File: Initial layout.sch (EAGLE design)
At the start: 32 parts, among them U2 TPS54540DDARQ1

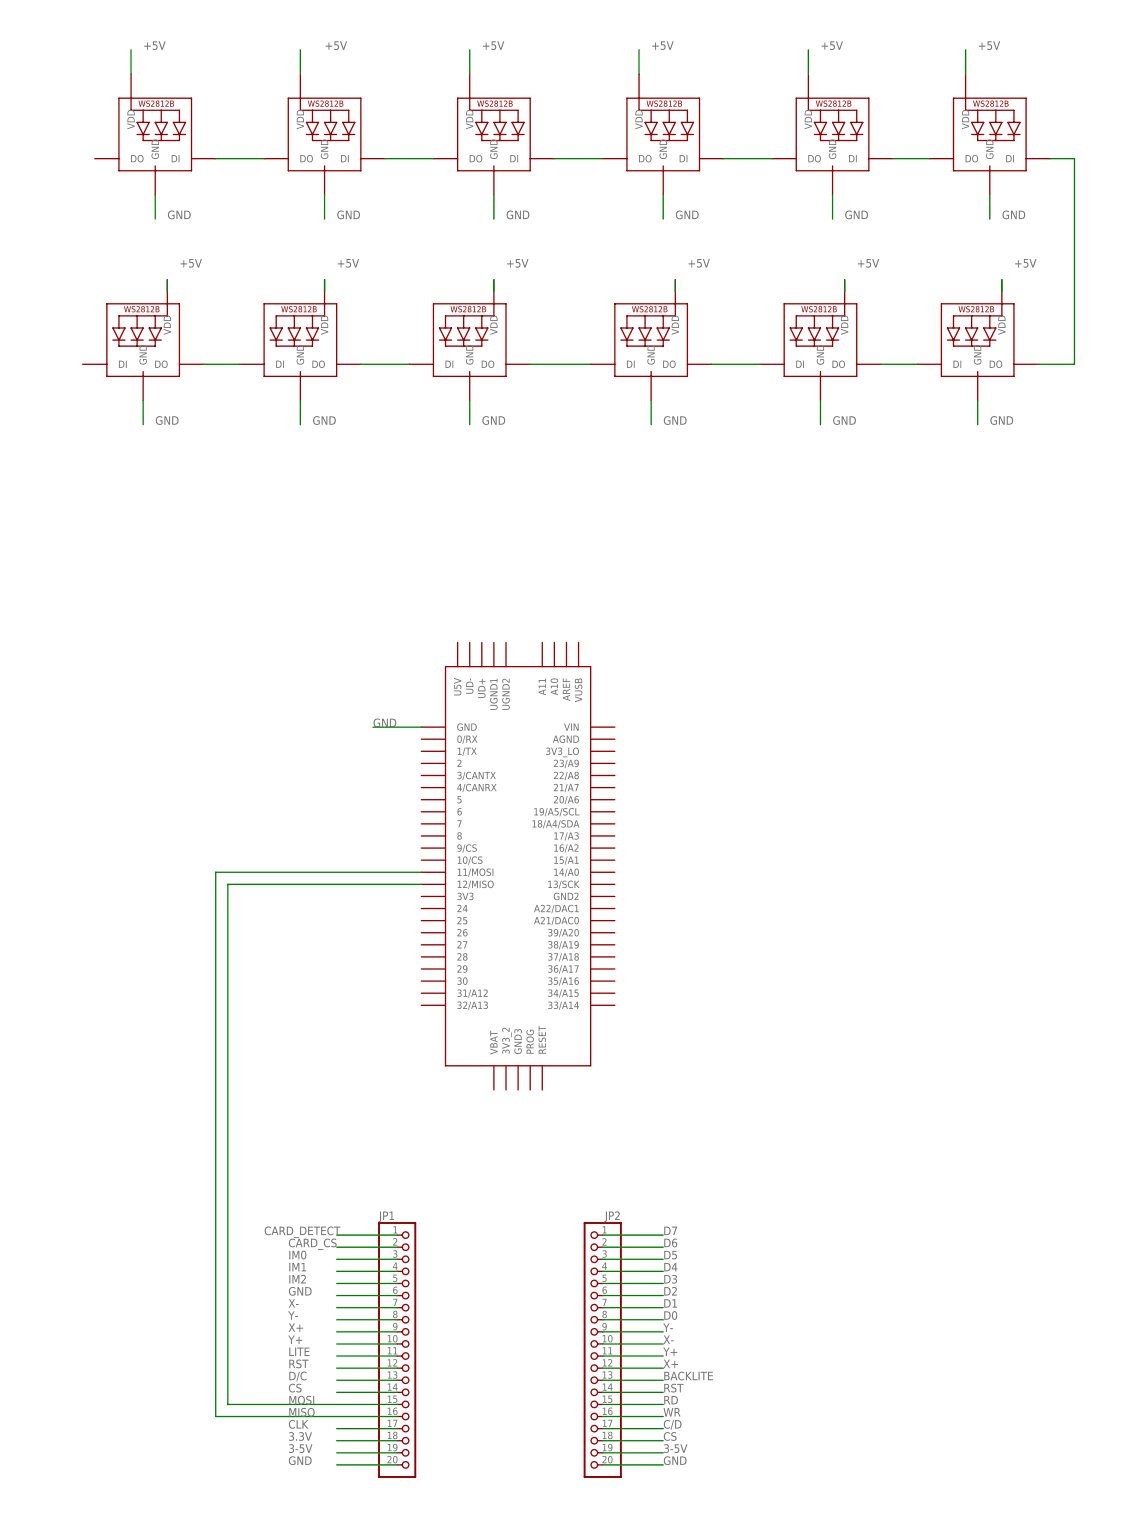
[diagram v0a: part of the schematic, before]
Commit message: Worked on schematic. Connected some wires
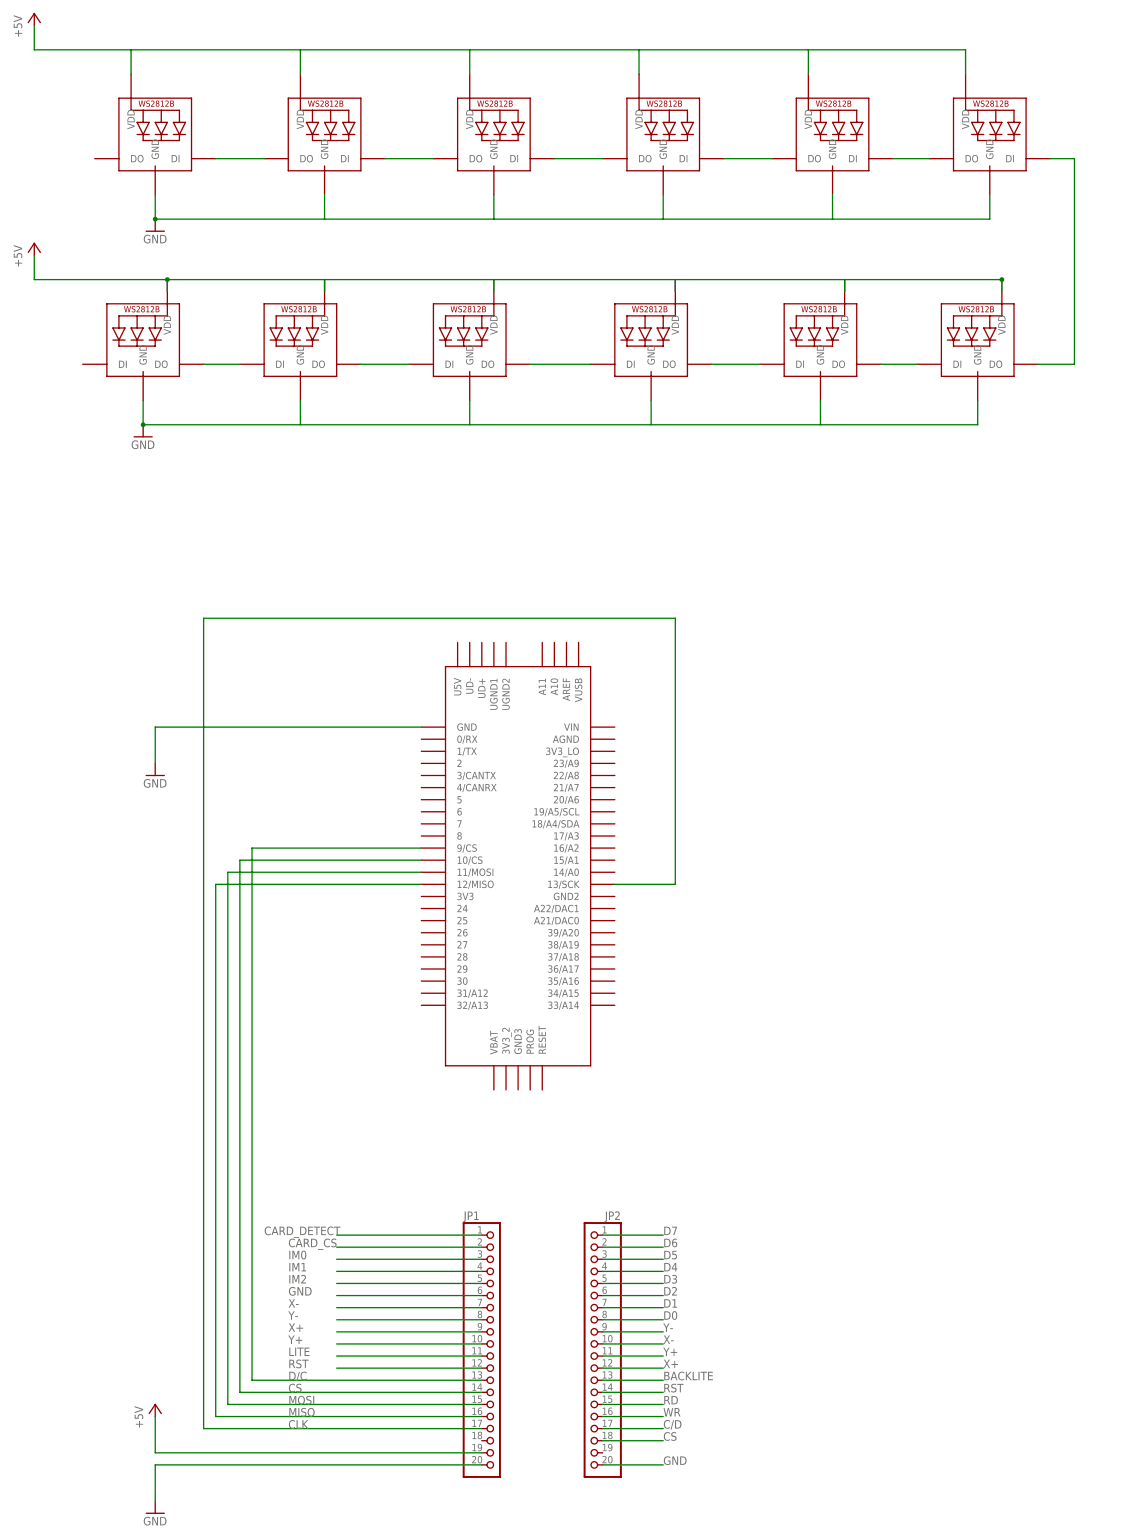
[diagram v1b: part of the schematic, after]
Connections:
- removed net 3-5V: JP1.19, JP2.19
- removed net 3.3V: JP1.18
- new net N$1: LED2.GND
- net +5V: now also JP1.19
- net CLK: now also U$2.13/SCK
- net CS: now also U$2.10/CS
- net D/C: now also U$2.9/CS
- net GND: no longer LED2.GND
- net MISO: now also U$2.12/MISO; no longer U$2.11/MOSI
- net MOSI: now also U$2.11/MOSI; no longer U$2.12/MISO
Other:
- moved on the sheet: JP1

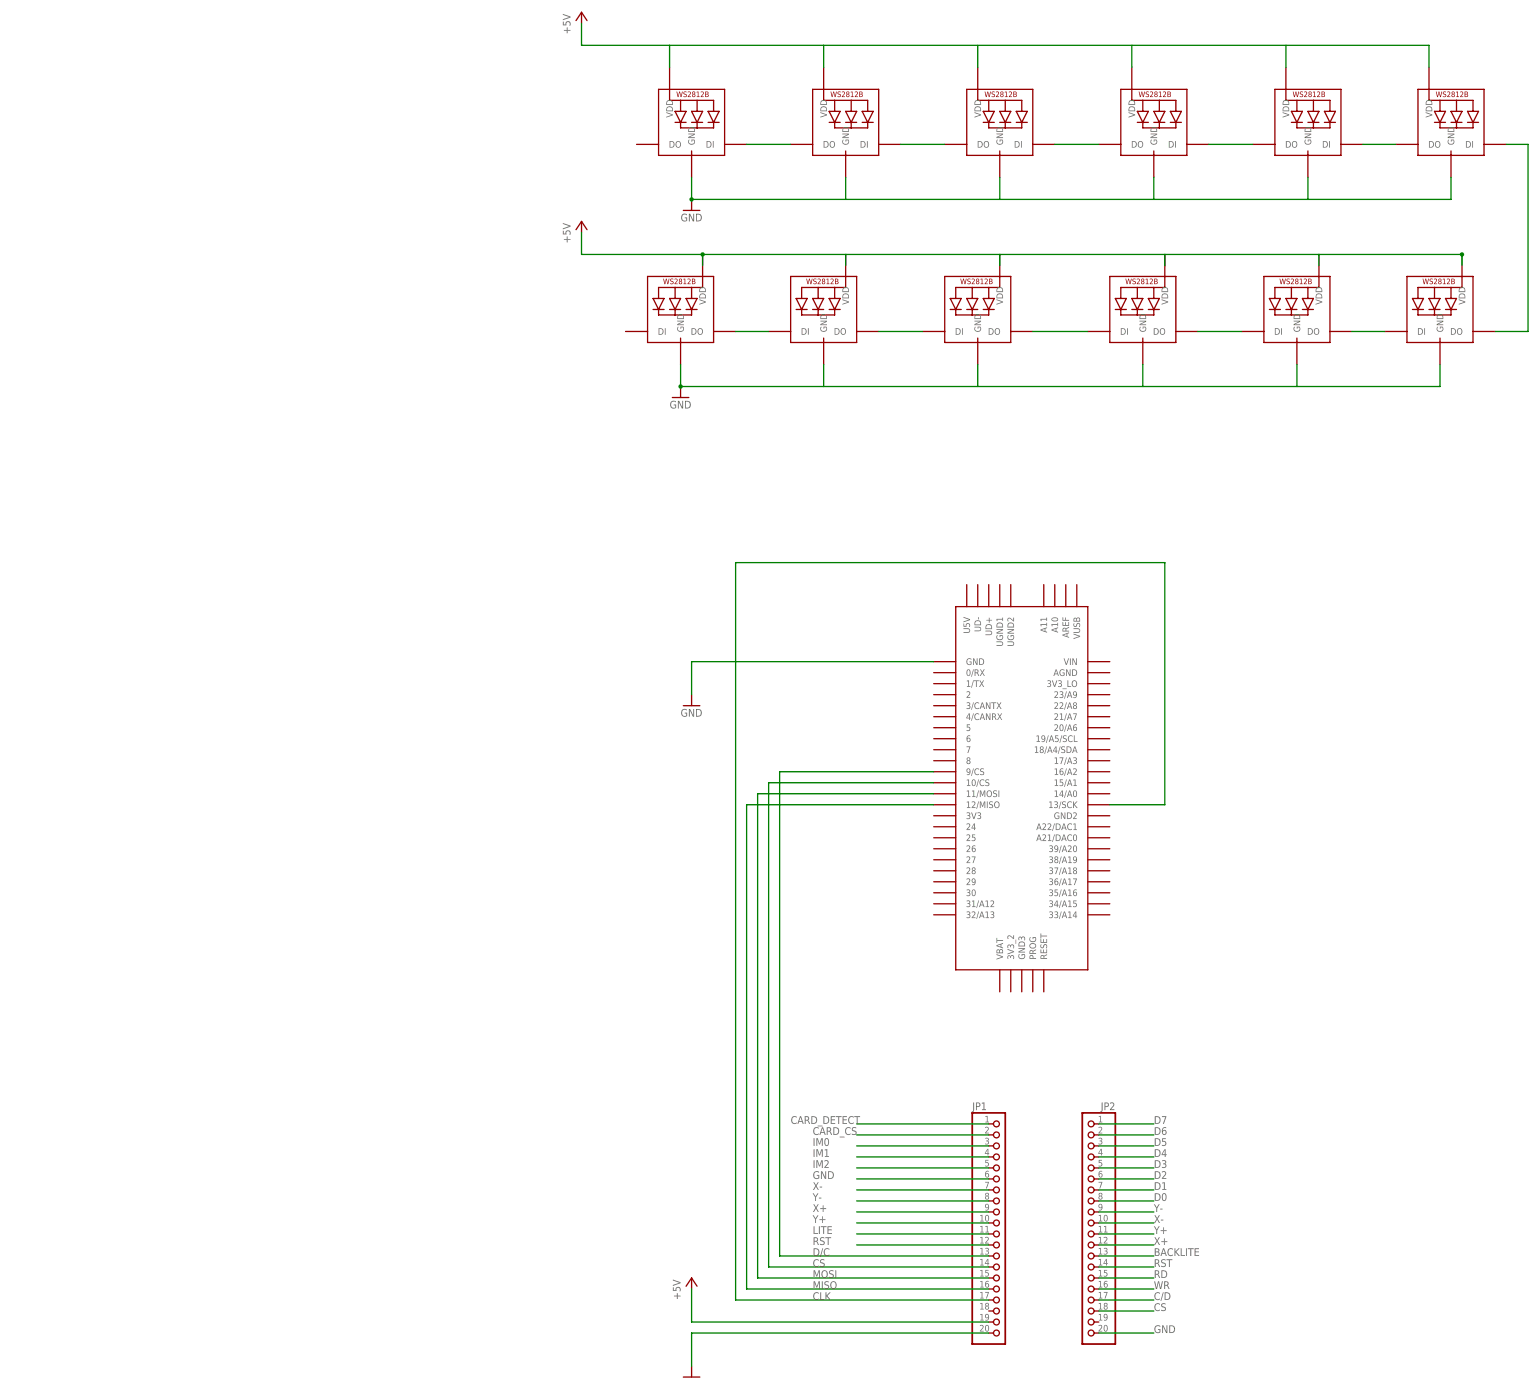
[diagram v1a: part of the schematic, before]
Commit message: Added some connectors.
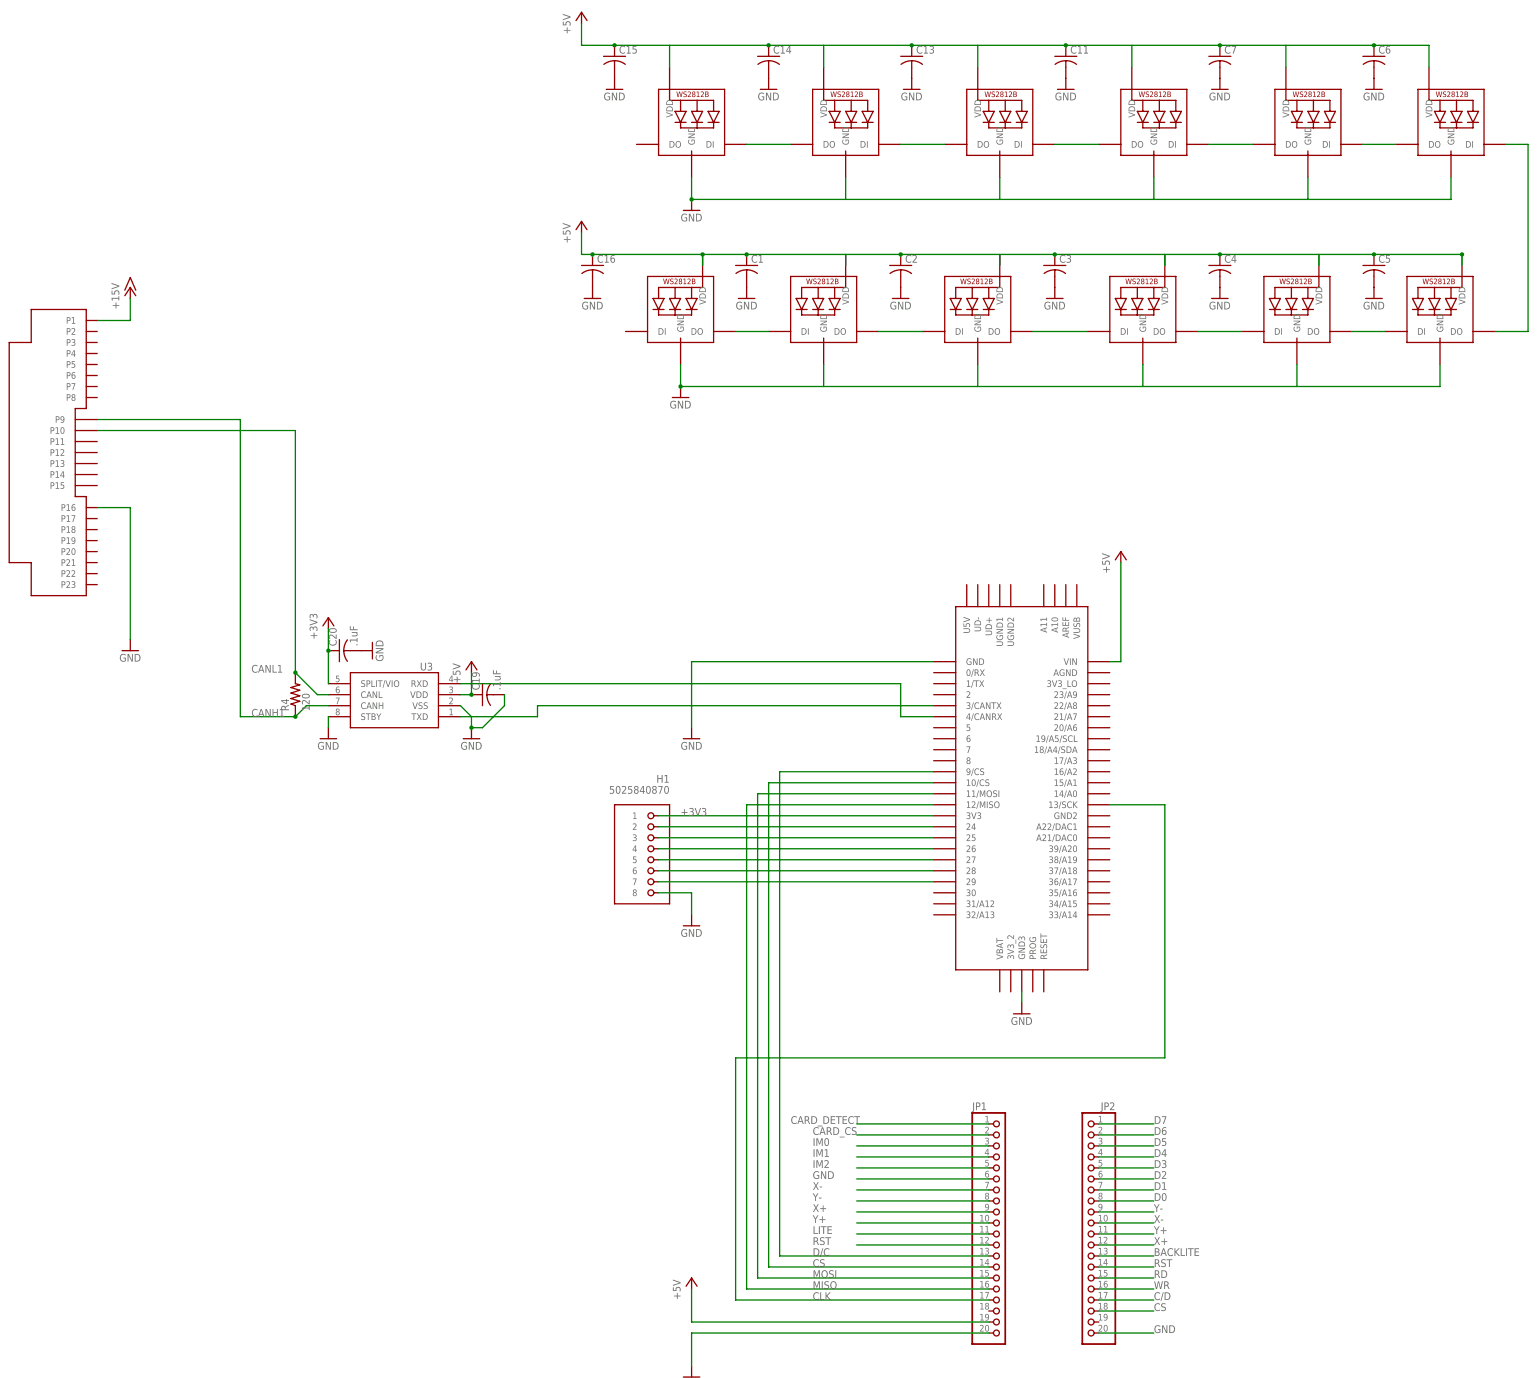
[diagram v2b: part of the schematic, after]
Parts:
- added C1, C11, C13, C14, C15, C16, C2, C3, C4, C5, C6, C7: (no value), rcl:C-USC0402
- added C19, C20: .1uF, rcl:C-USC0805
- added H1: 5025840870, FormE:MOLEX_CLICKMATE-8-VERTICAL
- added R4: 120, rcl:R-US_R0805
- added U$1: TE-776200-1, FormE:TE-776200-1
- added U3: (no value), FormE:MCP256X-SOIC
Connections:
- new net +3V3: C20.1, H1.1, U$2.3V3, U3.SPLIT/VIO
- new net CANH1: R4.1, U$1.P9, U3.CANH
- new net CANL1: R4.2, U$1.P10, U3.CANL
- new net N$11: H1.2, U$2.24
- new net N$13: H1.3, U$2.25
- new net N$15: H1.4, U$2.26
- new net N$17: H1.5, U$2.27
- new net N$18: H1.6, U$2.28
- new net N$19: H1.7, U$2.29
- new net N$25: U$2.4/CANRX, U3.RXD
- new net N$26: U$2.3/CANTX, U3.TXD
- net +15V: now also U$1.P1
- net +5V: now also C1.1, C11.1, C13.1, C14.1, C15.1, C16.1, C19.1, C2.1, C3.1, C4.1, C5.1, C6.1, C7.1, U$2.VIN, U3.VDD
- net GND: now also C1.2, C11.2, C13.2, C14.2, C15.2, C16.2, C19.2, C2.2, C20.2, C3.2, C4.2, C5.2, C6.2, C7.2, H1.8, U$1.P16, U$2.GND3, U3.STBY, U3.VSS

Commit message: Gave Mike an Analog Line
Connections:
- removed net N$19: H1.7, U$2.29
- new net N$3: H1.7, U$2.31/A12
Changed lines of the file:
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@@
-</segment>
-</net>
-<net name="N$19" class="0">
-<segment>
-<pinref part="U$2" gate="G$1" pin="29"/>
-<pinref part="H1" gate="G$1" pin="7"/>
-<wire x1="233.68" y1="-274.32" x2="170.18" y2="-274.32" width="0.1524" layer="91"/>
 </segment>
 </net>
@@
 </segment>
 </net>
+<net name="N$3" class="0">
+<segment>
+<pinref part="H1" gate="G$1" pin="7"/>
+<wire x1="170.18" y1="-274.32" x2="205.74" y2="-274.32" width="0.1524" layer="91"/>
+<wire x1="205.74" y1="-274.32" x2="205.74" y2="-279.4" width="0.1524" layer="91"/>
+<pinref part="U$2" gate="G$1" pin="31/A12"/>
+<wire x1="205.74" y1="-279.4" x2="233.68" y2="-279.4" width="0.1524" layer="91"/>
+</segment>
+</net>

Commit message: Worked on connecor pin
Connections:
- new net AMS: U$1.P20, U$2.5
- new net BSPD: U$1.P22, U$2.7
- new net IMD: U$1.P21, U$2.6
- new net N$16: U$2.3V3
- new net N$19: U$2.24
- new net N$20: H1.2
- new net N$21: H1.3
- new net N$22: H1.4
- new net N$23: H1.5
- new net N$24: H1.6
- new net N$27: LED1.DI, U$2.2
- new net SW_BIT0: U$1.P13, U$2.14/A0
- new net SW_BIT1: U$1.P14, U$2.15/A1
- new net SW_BIT2: U$1.P15, U$2.16/A2
- new net SW_BIT3: U$1.P17, U$2.17/A3
- new net TPS: U$1.P23, U$2.8
- net +3V3: no longer H1.1, U$2.3V3
- net +5V: now also U$1.P18
- net CANH1: now also U$1.P10; no longer U$1.P9
- net CANL1: now also U$1.P9; no longer U$1.P10
- net GND: now also U$1.P19
- net N$11: now also H1.1; no longer H1.2, U$2.24
- net N$13: no longer H1.3
- net N$15: no longer H1.4
- net N$17: no longer H1.5
- net N$18: no longer H1.6
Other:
- note added: "3.5" TFT Display"
- note added: "Multi-function LED Display"
- note added: "Steering Wheel"
- moved on the sheet: C1, C10, C11, C12, C13, C14, C15, C16, C18, C19, C2, C20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

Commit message: Finished Schematic?? Probably.
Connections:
- new net LBL: U$1.P5, U$2.31/A12
- new net RTDL: U$1.P4, U$2.30
- new net SERVO_PWM: U$1.P3, U$2.29
- net +5V: now also U$1.P2
- net GND: now also U$1.P6
- net N$3: now also U$2.32/A13; no longer U$2.31/A12
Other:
- moved on the sheet: C1, C10, C11, C12, C13, C14, C15, C16, C18, C2, C24, C25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

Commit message: Rough board work
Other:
- note added: "23 Pin Ampseal"
- note added: "CAN Transiever"
- note added: "Constant Current Power Supply"
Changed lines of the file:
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@@
 <?xml version="1.0" encoding="utf-8"?>
 <!DOCTYPE eagle SYSTEM "eagle.dtd">
-<eagle version="8.4.1">
+<eagle version="8.6.0">
 <drawing>
 <settings>
@@
 <plain>
 <text x="391.16" y="-83.82" size="1.778" layer="91">7443251000</text>
-<text x="137.16" y="-358.14" size="1.778" layer="91" rot="MR0">Steering Wheel</text>
-<text x="124.46" y="-45.72" size="1.778" layer="91">Multi-function LED Display</text>
-<text x="254" y="-355.6" size="1.778" layer="91">3.5" TFT Display</text>
+<text x="149.86" y="-358.14" size="3.81" layer="91" rot="MR0">Steering Wheel</text>
+<text x="81.28" y="-45.72" size="7.62" layer="91">Multi-function LED Display</text>
+<text x="223.52" y="-355.6" size="7.62" layer="91">3.5" TFT Display</text>
+<text x="381" y="-193.04" size="7.62" layer="91">23 Pin Ampseal</text>
+<text x="337.82" y="-45.72" size="7.62" layer="91">Constant Current Power Supply</text>
+<text x="12.7" y="-358.14" size="3.81" layer="91">CAN Transiever</text>
 </plain>
 <instances>
@@
 </segment>
 </net>
+<net name="N$33" class="0">
+<segment>
+<wire x1="350.52" y1="-195.58" x2="350.52" y2="-297.18" width="0.1524" layer="91"/>
+<wire x1="350.52" y1="-297.18" x2="467.36" y2="-297.18" width="0.1524" layer="91"/>
+<wire x1="467.36" y1="-297.18" x2="467.36" y2="-195.58" width="0.1524" layer="91"/>
+<wire x1="467.36" y1="-195.58" x2="350.52" y2="-195.58" width="0.1524" layer="91"/>
+</segment>
+</net>
